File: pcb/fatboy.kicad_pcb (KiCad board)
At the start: 2 copper layers, 232.2 x 108.2 mm, 76 parts, among them SW1 SW_Push, U1 Helios

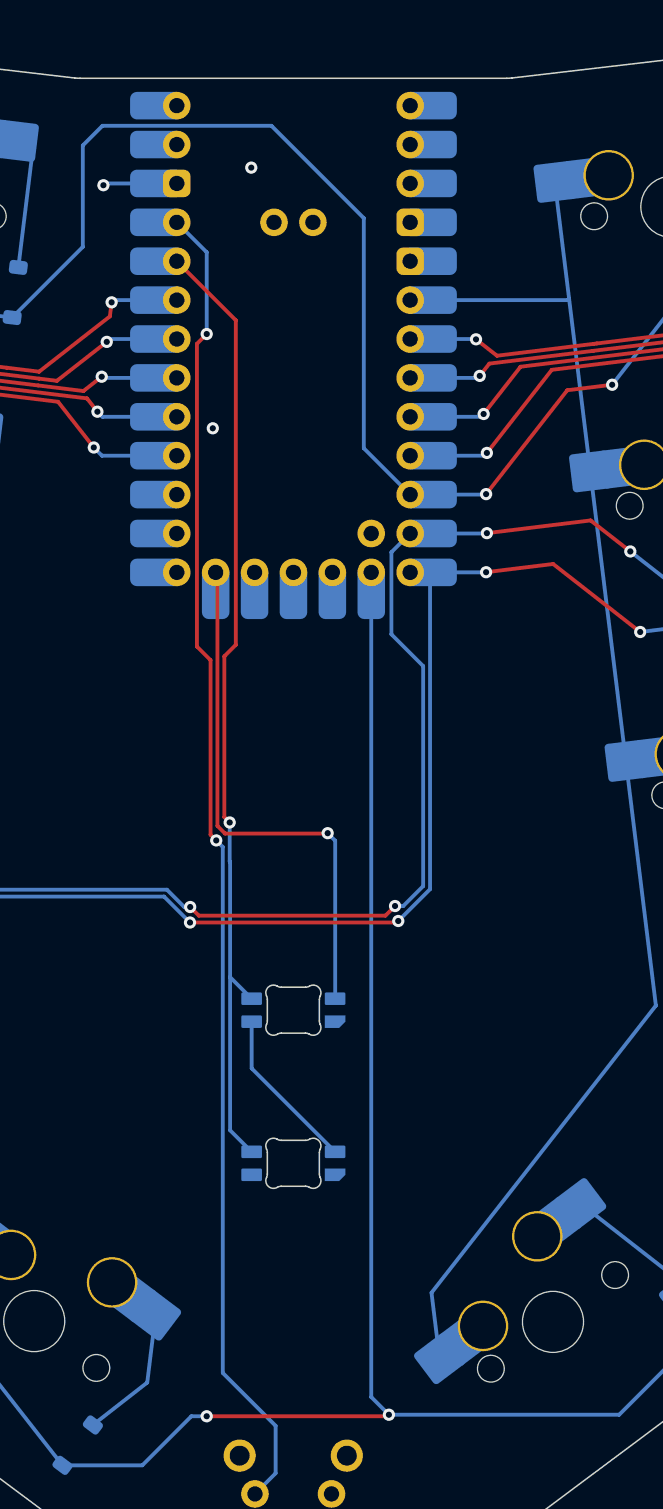
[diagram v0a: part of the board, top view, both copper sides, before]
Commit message: update helios footprint
Signed-off-by: Anant Thazhemadam <anant.thazhemadam@gmail.com>
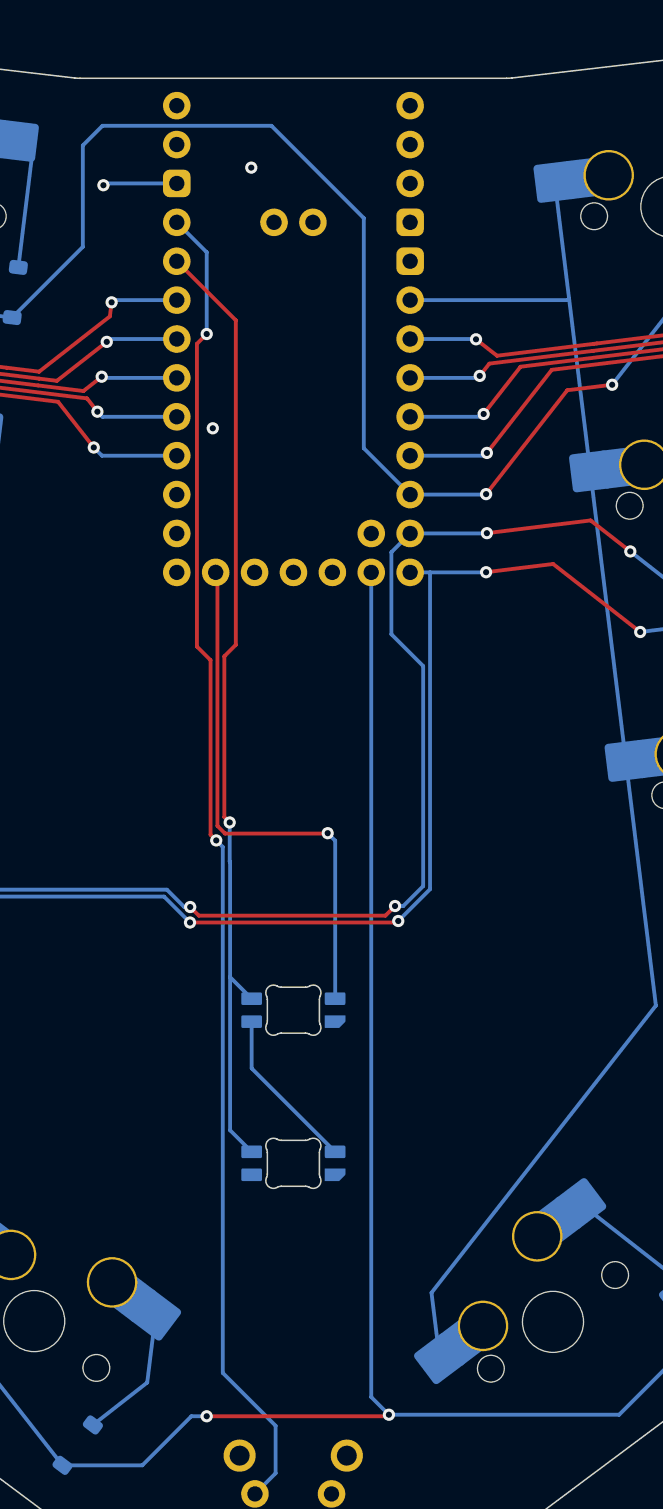
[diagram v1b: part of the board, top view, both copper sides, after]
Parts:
- U1: footprint PCM_marbastlib-xp-promicroish:Helios_ACH -> PCM_marbastlib-xp-promicroish:Helios_AH_USBup
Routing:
- net COL10: track 131.9 -> 133.2 mm
- net ROW2: track 271.1 -> 272.4 mm
- net COL5: track 102.9 -> 104.2 mm
- net COL3: track 138.7 -> 140.0 mm
- net COL2: track 124.7 -> 126.0 mm
- net COL1: track 148.7 -> 150.0 mm
- net COL4: track 116.1 -> 117.4 mm
- net ROW4: track 186.7 -> 188.0 mm
- net COL7: track 103.8 -> 105.1 mm
- net COL6: track 91.4 -> 92.7 mm
- net ROW3: track 266.7 -> 268.0 mm
- net ROW1: track 253.8 -> 255.1 mm
- net COL9: track 112.0 -> 113.3 mm
- net COL8: track 126.0 -> 127.3 mm

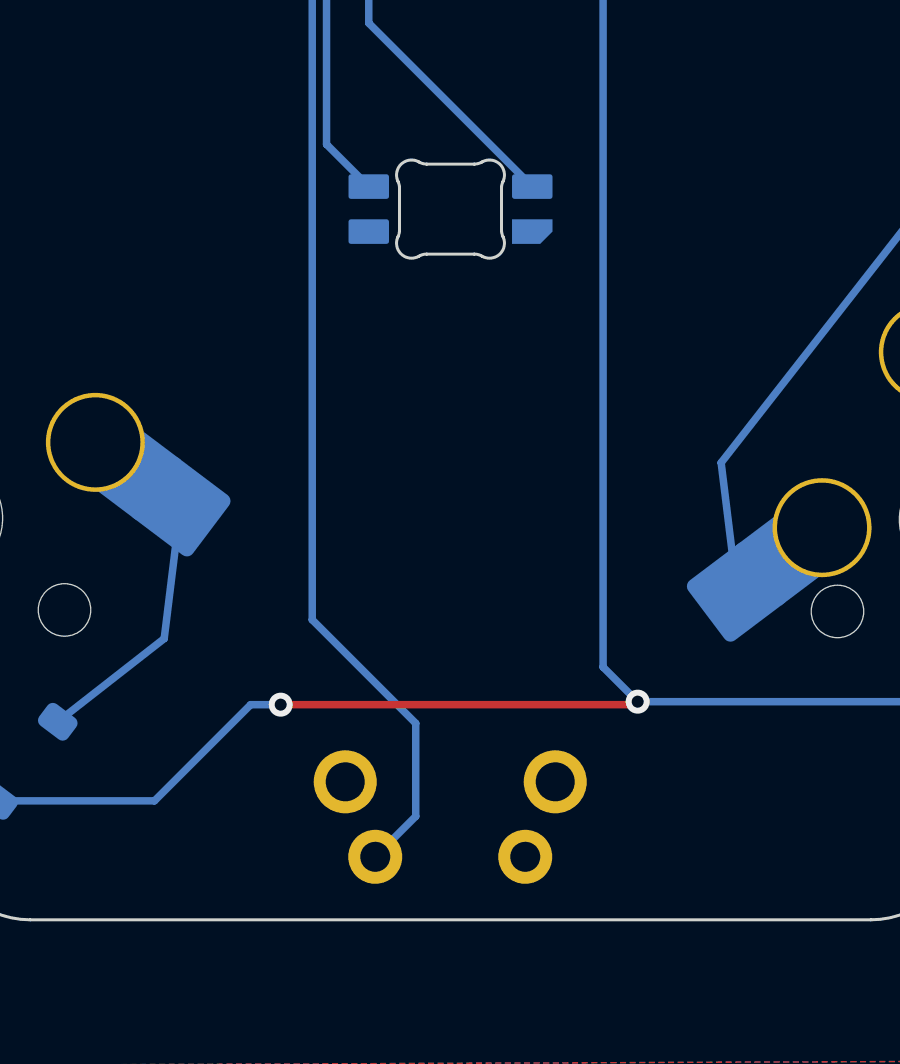
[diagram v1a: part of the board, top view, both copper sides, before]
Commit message: update reset switch footprint
Signed-off-by: Anant Thazhemadam <anant.thazhemadam@gmail.com>
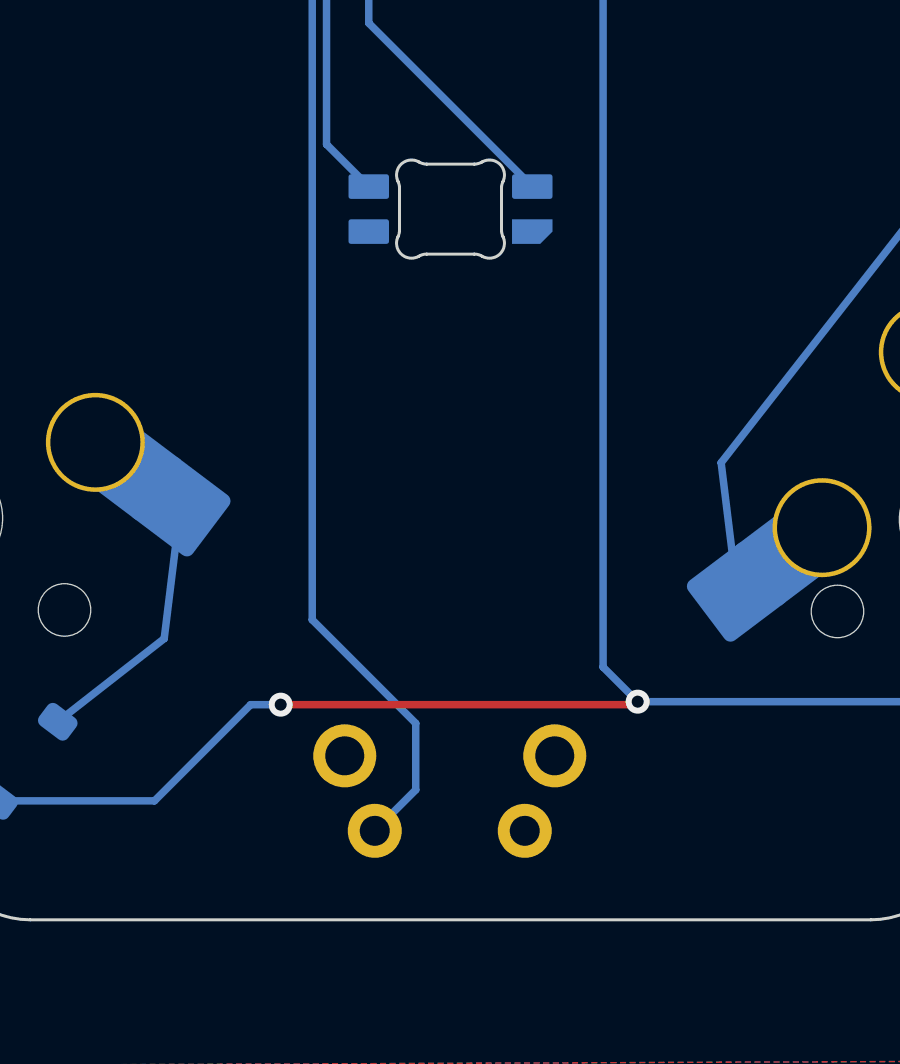
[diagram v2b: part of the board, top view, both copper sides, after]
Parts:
- SW1: footprint fatboy:top_reset -> PCM_marbastlib-various:SW_SKHLLCA010
- moved SW1 0.87 mm to (195.7, 190.5)
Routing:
- net RESET: track 86.8 -> 85.9 mm
